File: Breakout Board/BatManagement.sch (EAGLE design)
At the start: 23 parts, among them J1 RASPBERRYPI-40-PIN-GPIO_PTH, SW1 100SP1T2B4M6QE, X3 22-23-2031, X4 22-23-2031

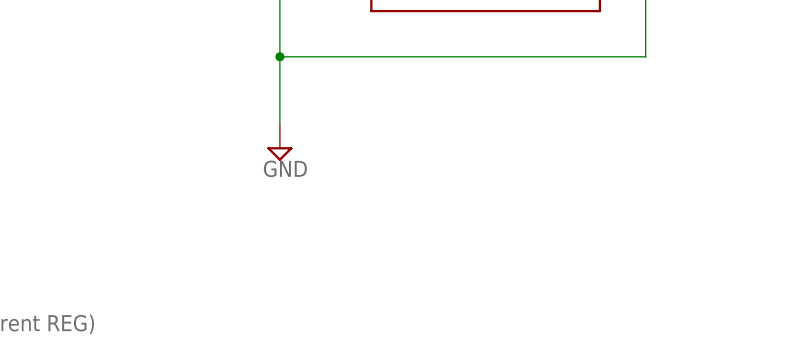
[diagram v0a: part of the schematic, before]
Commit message: Added jumper to breakout2
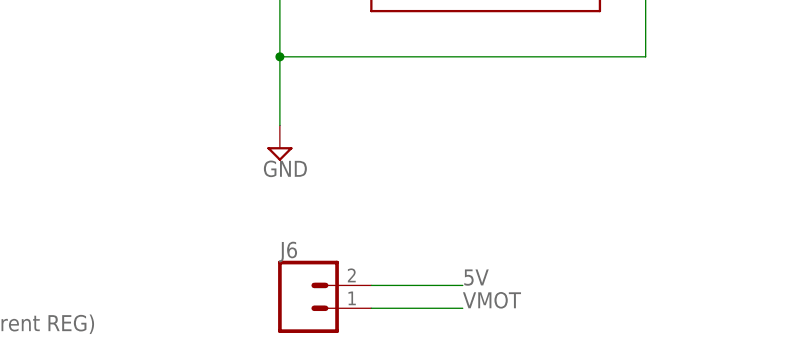
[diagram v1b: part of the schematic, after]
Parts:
- added J6: (no value), SparkFun-Connectors:CONN_02
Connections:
- net 5V: now also J6.2
- net VMOT: now also J6.1
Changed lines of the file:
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@@
 <part name="J5" library="SparkFun-Connectors" library_urn="urn:adsk.eagle:library:513" deviceset="CONN_06" device="SILK_FEMALE_PTH" package3d_urn="urn:adsk.eagle:package:38009/1"/>
 <part name="SUPPLY15" library="supply2" library_urn="urn:adsk.eagle:library:372" deviceset="GND" device=""/>
+<part name="J6" library="SparkFun-Connectors" library_urn="urn:adsk.eagle:library:513" deviceset="CONN_02" device="" package3d_urn="urn:adsk.eagle:package:38039/1"/>
 </parts>
 <sheets>
@@
 <instance part="SUPPLY15" gate="GND" x="337.82" y="88.9" smashed="yes">
 <attribute name="VALUE" x="335.915" y="85.725" size="1.778" layer="96"/>
+</instance>
+<instance part="J6" gate="G$1" x="101.6" y="-27.94" smashed="yes">
+<attribute name="VALUE" x="99.06" y="-32.766" size="1.778" layer="96" font="vector"/>
+<attribute name="NAME" x="99.06" y="-22.352" size="1.778" layer="95" font="vector"/>
 </instance>
 </instances>
@@
 <label x="180.34" y="101.6" size="1.778" layer="95"/>
 </segment>
+<segment>
+<pinref part="J6" gate="G$1" pin="1"/>
+<wire x1="109.22" y1="-27.94" x2="119.38" y2="-27.94" width="0.1524" layer="91"/>
+<label x="119.38" y="-27.94" size="1.778" layer="95"/>
+</segment>
 </net>
 <net name="LED1" class="0">
@@
 <label x="345.44" y="99.06" size="1.778" layer="95"/>
 </segment>
-</net>
+<segment>
+<pinref part="J6" gate="G$1" pin="2"/>
+<wire x1="109.22" y1="-25.4" x2="119.38" y2="-25.4" width="0.1524" layer="91"/>
+<label x="119.38" y="-25.4" size="1.778" layer="95"/>
+</segment>
+</net>
